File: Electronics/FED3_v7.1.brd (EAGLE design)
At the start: 108 x 50 mm, 51 parts, among them IC1 RTC_PCF8523T, IC2 TB6612 SSOP, IC3 M74VHC1GT50DTT1G, Q1 32.768, Q2 DMG3415, SW1 SSSS811101, X1 B2B-PH-K-S(LF)(SN)

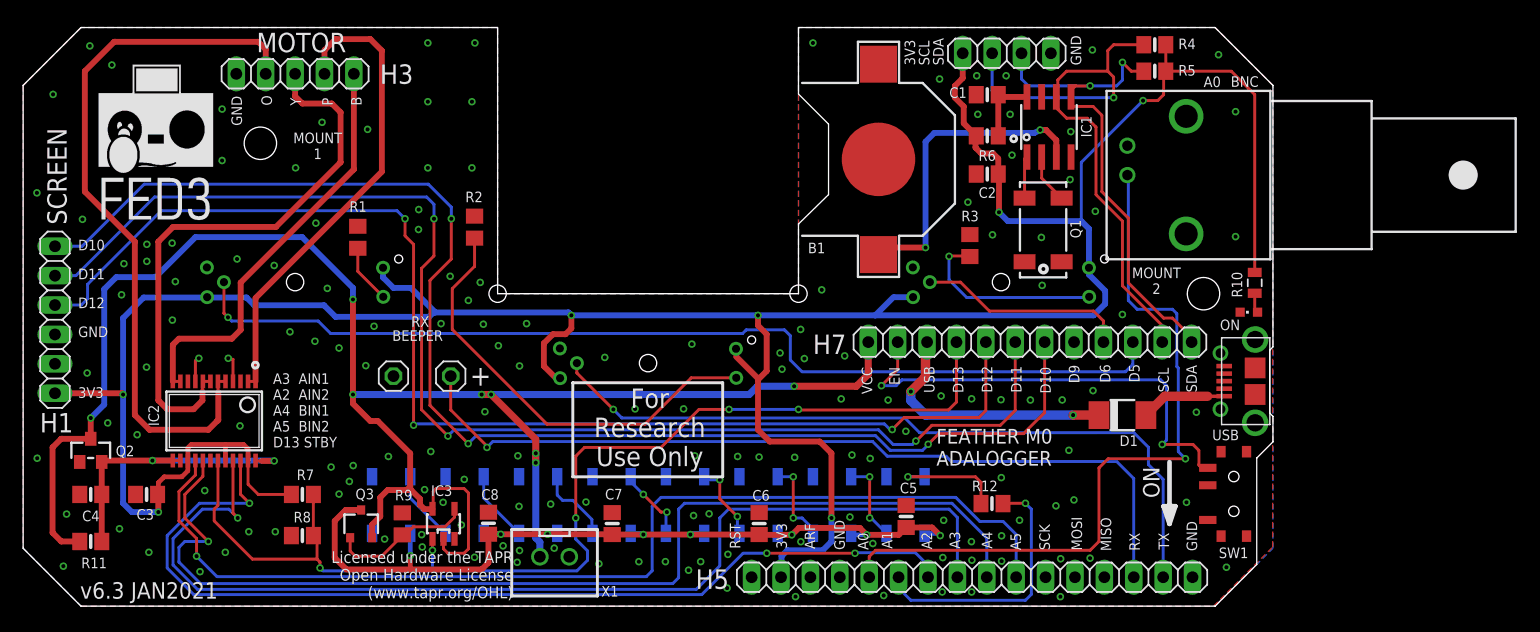
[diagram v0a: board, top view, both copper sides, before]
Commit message: Added two extra RGBs, replaced the BNC with an audio socket, and updated the license.
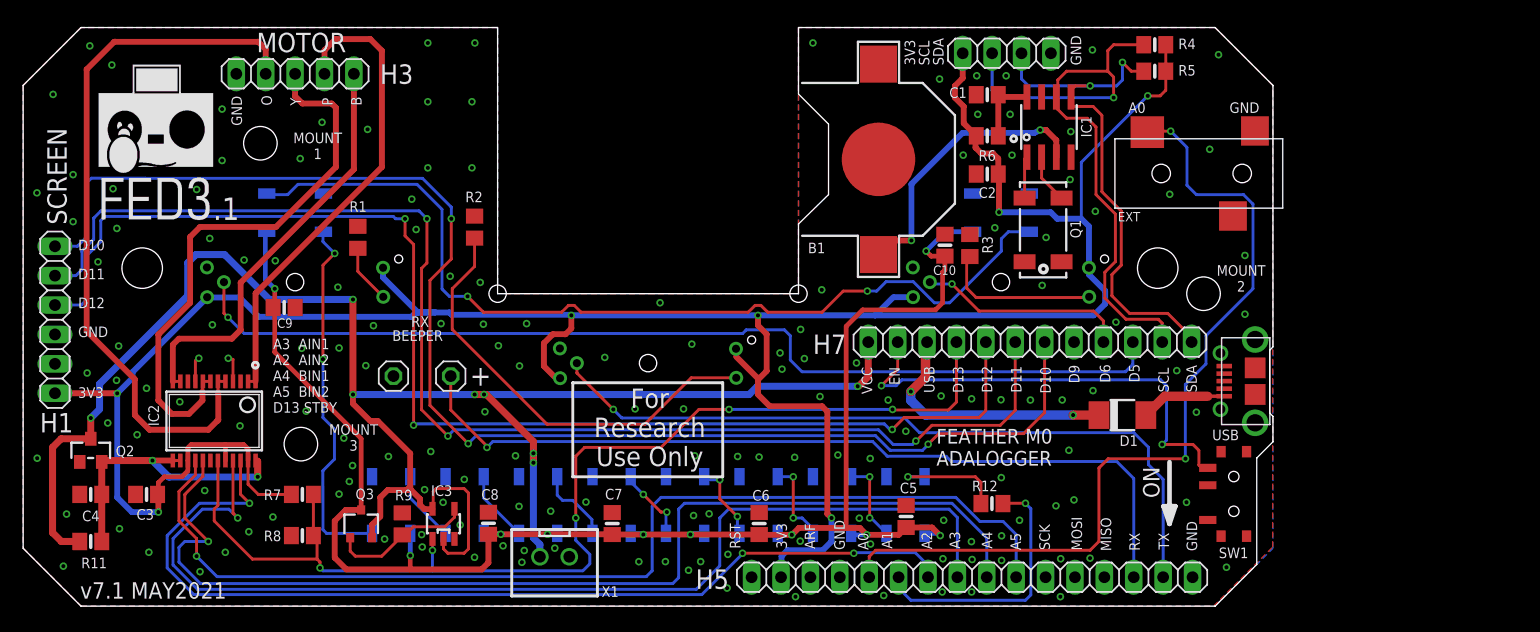
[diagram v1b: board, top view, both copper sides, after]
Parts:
- removed BNC: BNC, CNP-connectors:BNC_RA
- removed ON: (no value), led:CHIPLED_0603
- removed R10: 1k3, SparkFun:0805
- added C10, C9: 10uF, microbuilder:0805-NO
- added EXT: (no value), CNP-connectors:35RASMT2BHNTRX
- added LED10, LED9: WS2812B5050, microbuilder:WS2812B
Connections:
- removed net N$8: ON.A, R10.1
- new net N$17: LED10.4-DIN, LED9.2-DOUT
- new net N$18: LED8.2-DOUT, LED9.4-DIN
- net 3V3: no longer R10.2
- net A0: now also EXT.4; no longer BNC.1
- net GND: now also C10.2, C9.2, EXT.5, LED10.3-GND, LED9.3-GND; no longer BNC.2, ON.C
- net VCCNEO: now also C10.1, C9.1, LED10.1-VDD, LED9.1-VDD
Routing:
- net N$17: track 0.00 -> 80.9 mm, vias 0 -> 2
- net VCCNEO: track 74.4 -> 139.4 mm, vias 8 -> 10
- net N$18: track 0.00 -> 31.8 mm, vias 0 -> 2
- net 3V3: track 262.7 -> 235.2 mm
- net A0: track 64.7 -> 76.3 mm, vias 1 -> 2
- net VCC: track 160.6 -> 156.3 mm
- net D10: track 118.0 -> 121.1 mm
- net N$3: track 16.7 -> 13.8 mm, vias 1 -> 0
- net VBAT1: track 26.9 -> 24.5 mm
- net SCL: track 53.8 -> 56.1 mm
- net SDA: track 44.5 -> 46.6 mm
- net D12: track 109.1 -> 111.2 mm
- net N$8: track 1.74 -> 0.00 mm
- net YELLOW: track 49.8 -> 48.4 mm
- net VMOTOR: track 25.9 -> 25.0 mm
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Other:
- board text added: ".1"
- board text added: "MOUNT 3"
- board text added: "v7.1 MAY2021"
- board text removed: "Licensed under the TAPR Open Hardware License (www.tapr.org/OHL)"
- board text removed: "Licensed under the TAPR Open Hardware License (www.tapr.org/OHL) Copyright 2019 Mohamed Ali, FIlipe Carvalho, Alexxai Kravitz"
- board text removed: "v6.3 JAN2021"
